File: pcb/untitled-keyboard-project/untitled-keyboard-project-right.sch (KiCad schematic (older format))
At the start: 64 parts, among them J1 USB_mini_micro_B, K1 KEYSW, K10 KEYSW, K11 KEYSW, K12 KEYSW, K13 KEYSW, K14 KEYSW, K15 KEYSW, K16 KEYSW, K17 KEYSW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

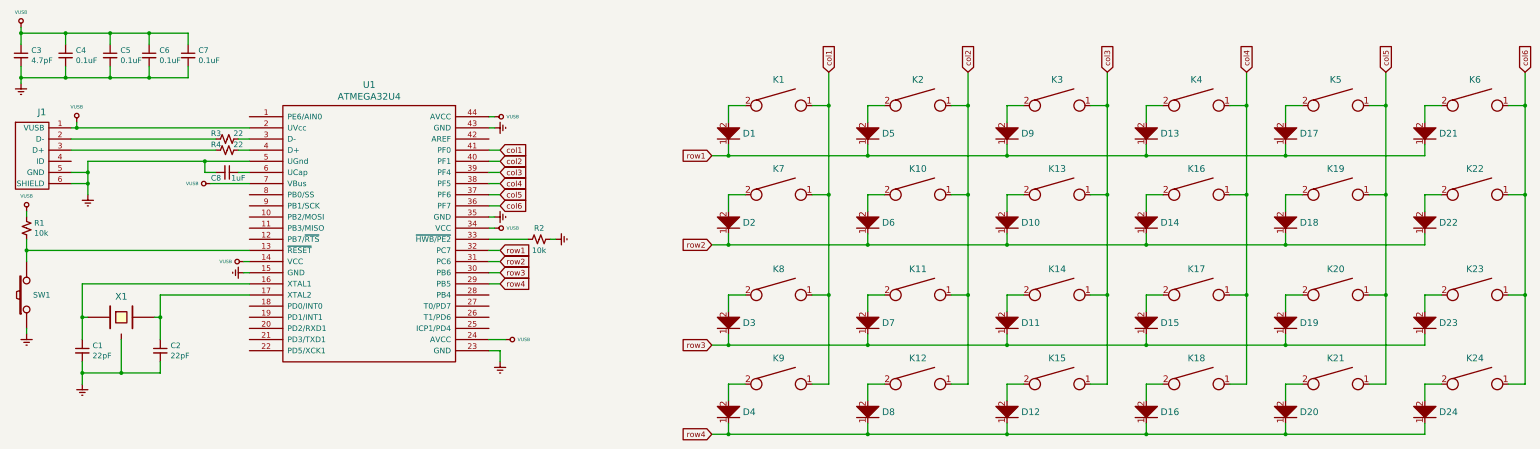
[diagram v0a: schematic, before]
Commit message: Update 12/18/19 00:36
Fixed net labels and assigned footprints to schematic symbols.
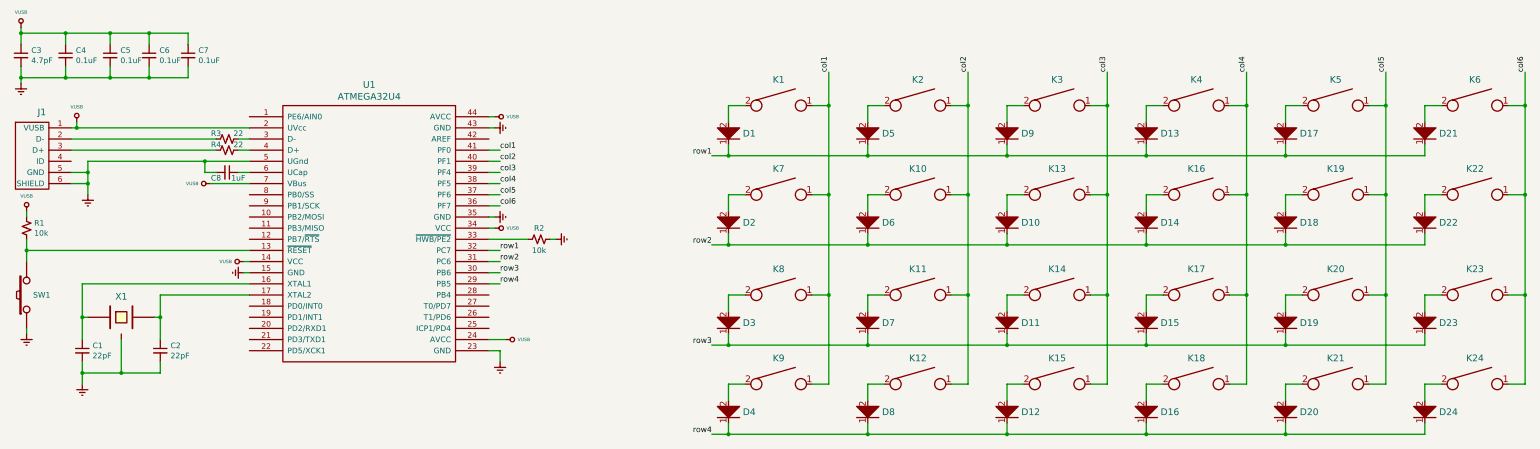
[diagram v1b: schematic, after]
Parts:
- C1, C2, C3, C4, C5, C6, C7, C8: footprint (none) -> Capacitor_SMD:C_0805_2012Metric
- R1, R2, R3, R4: footprint (none) -> Resistor_SMD:R_0805_2012Metric
- SW1: footprint (none) -> Button_Switch_SMD:SW_SPST_TL3342
- U1: footprint (none) -> Package_QFP:TQFP-44_10x10mm_P0.8mm
